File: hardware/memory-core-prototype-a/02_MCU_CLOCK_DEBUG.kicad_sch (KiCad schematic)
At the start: 1 part, among them J902 SHEET_INTERFACE_NOT_FITTED

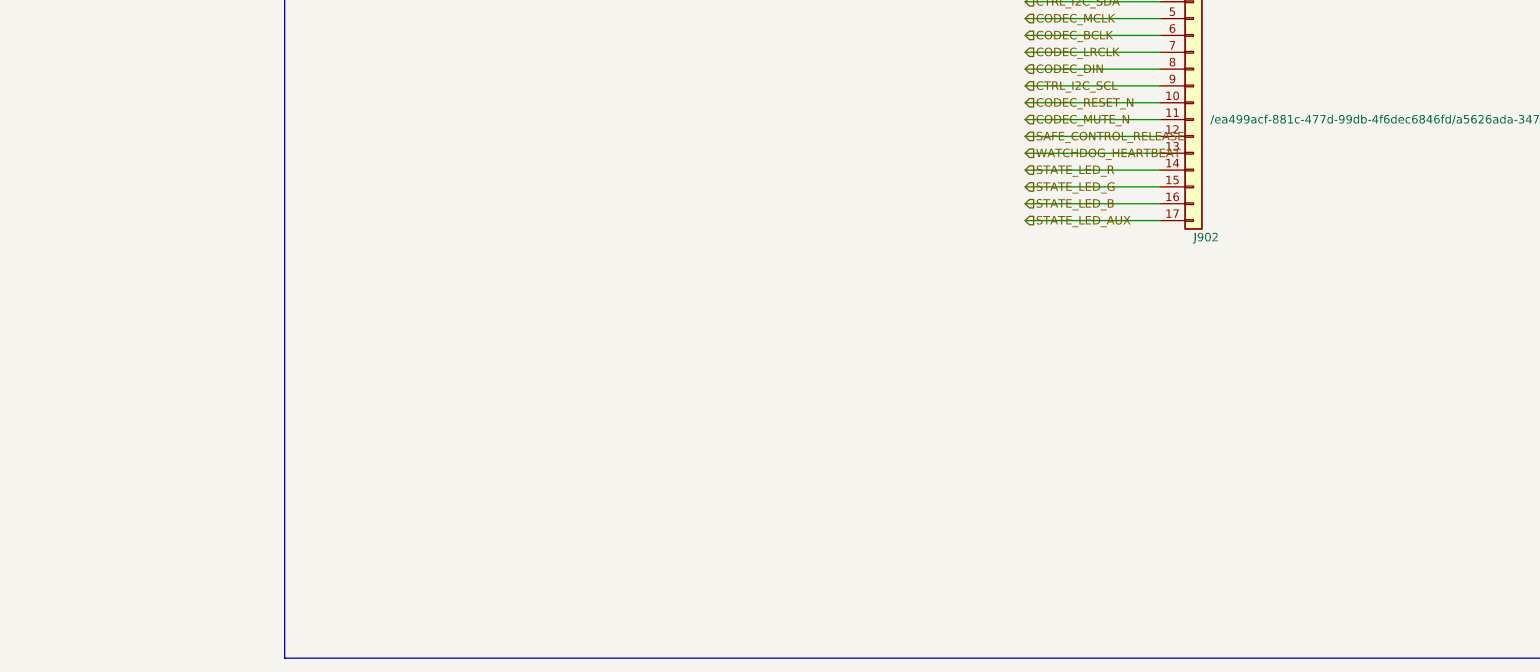
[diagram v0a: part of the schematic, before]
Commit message: Capture ERC-validated controls and state sheet
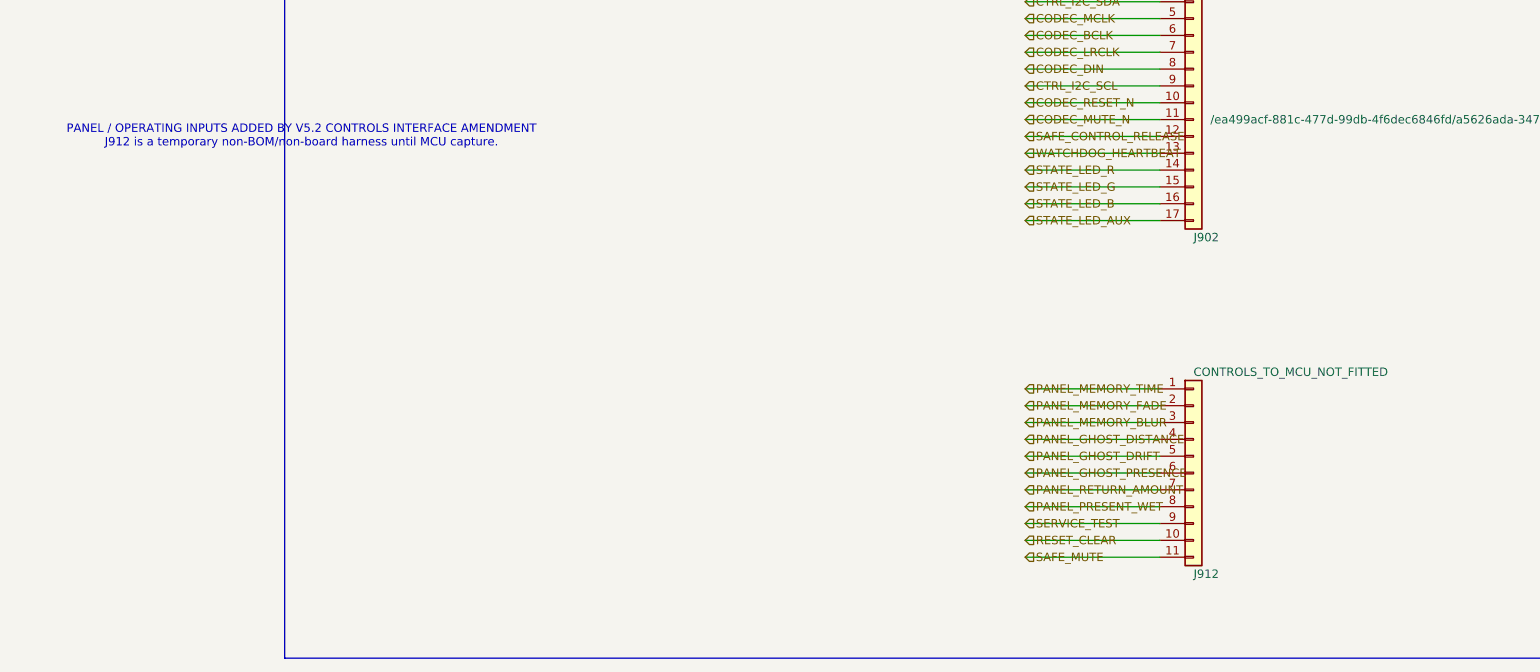
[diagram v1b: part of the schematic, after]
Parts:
- added J912: CONTROLS_TO_MCU_NOT_FITTED, symbol Connector_Generic:Conn_01x11
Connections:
- new net PANEL_GHOST_DISTANCE: J912.4 (Pin_4)
- new net PANEL_GHOST_DRIFT: J912.5 (Pin_5)
- new net PANEL_GHOST_PRESENCE: J912.6 (Pin_6)
- new net PANEL_MEMORY_BLUR: J912.3 (Pin_3)
- new net PANEL_MEMORY_FADE: J912.2 (Pin_2)
- new net PANEL_MEMORY_TIME: J912.1 (Pin_1)
- new net PANEL_PRESENT_WET: J912.8 (Pin_8)
- new net PANEL_RETURN_AMOUNT: J912.7 (Pin_7)
- new net RESET_CLEAR: J912.10 (Pin_10)
- new net SAFE_MUTE: J912.11 (Pin_11)
- new net SERVICE_TEST: J912.9 (Pin_9)
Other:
- note added: "PANEL / OPERATING INPUTS ADDED BY V5.2 CONTROLS INTERFACE AMENDMENT J912 is a temporary non-BOM/non-board harness until MCU capture."

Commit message: Capture ERC-validated MCU clock and debug sheet
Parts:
- removed J902: SHEET_INTERFACE_NOT_FITTED, symbol Connector_Generic:Conn_01x17
- removed J912: CONTROLS_TO_MCU_NOT_FITTED, symbol Connector_Generic:Conn_01x11
- added C201, C202, C203, C204, C205, C208, C211, C212: 100nF, Capacitor_SMD:C_0805_2012Metric, symbol Device:C
- added C206: 4.7µF, Capacitor_SMD:C_0805_2012Metric, symbol Device:C
- added C207: 1µF, Capacitor_SMD:C_0805_2012Metric, symbol Device:C
- added C209, C210: 2.2µF low-ESR, Capacitor_SMD:C_0805_2012Metric, symbol Device:C
- added FB20: 600Ω@100MHz provisional, symbol Device:L_Ferrite
- added J20: SWD SERVICE, symbol Connector_Generic:Conn_01x05
- added R200: 33Ω series, Resistor_SMD:R_0805_2012Metric, symbol Device:R
- added R201: 100k reset default low, Resistor_SMD:R_0805_2012Metric, symbol Device:R
- added R202: 100k mute default low, Resistor_SMD:R_0805_2012Metric, symbol Device:R
- added R203: 100k BOOT0 pull-down, Resistor_SMD:R_0805_2012Metric, symbol Device:R
- added TP200: HSE_24M576, symbol Connector:TestPoint
- added TP201: BOOT0, symbol Connector:TestPoint
- added TP202: CODEC_MCLK, symbol Connector:TestPoint
- added TP203: CODEC_BCLK, symbol Connector:TestPoint
- added TP204: CODEC_LRCLK, symbol Connector:TestPoint
- added TP205: CODEC_DIN, symbol Connector:TestPoint
- added TP206: CODEC_DOUT, symbol Connector:TestPoint
- added TP207: I2C_SCL, symbol Connector:TestPoint
- added TP208: I2C_SDA, symbol Connector:TestPoint
- added TP209: WATCHDOG_HEARTBEAT, symbol Connector:TestPoint
- added TP210: FAULT_RESET_N, symbol Connector:TestPoint
- added TP211: SAFE_RELEASE, symbol Connector:TestPoint
- added TP212: MCU_ANALOG_3V3, symbol Connector:TestPoint
- added U10: STM32H743VIT6, symbol MerrinLab_PrototypeA:STM32H743VIT6_LQFP100
- added U11: 24.576MHz 3V3 CMOS OSC, symbol MerrinLab_PrototypeA:OSC_CMOS_4PIN
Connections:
- net CODEC_BCLK: now also TP203.1, U10.4 (PE5)
- net CODEC_DIN: now also TP205.1, U10.5 (PE6)
- net CODEC_DOUT: now also TP206.1, U10.2 (PE3)
- net CODEC_LRCLK: now also TP204.1, U10.3 (PE4)
- net CODEC_MCLK: now also TP202.1, U10.1 (PE2)
- net CODEC_MUTE_N: now also R202.1, U10.56 (PD9)
- net CODEC_RESET_N: now also R201.1, U10.55 (PD8)
- net CTRL_I2C_SCL: now also TP207.1, U10.95 (PB8)
- net CTRL_I2C_SDA: now also TP208.1, U10.96 (PB9)
- net HARDWARE_FAULT_N: now also J20.4 (Pin_4), TP210.1, U10.14 (NRST), U10.57 (PD10)
- net PANEL_GHOST_DISTANCE: now also U10.25 (PA3)
- net PANEL_GHOST_DRIFT: now also U10.28 (PA4)
- net PANEL_GHOST_PRESENCE: now also U10.29 (PA5)
- net PANEL_MEMORY_BLUR: now also U10.24 (PA2)
- net PANEL_MEMORY_FADE: now also U10.23 (PA1)
- net PANEL_MEMORY_TIME: now also U10.22 (PA0)
- net PANEL_PRESENT_WET: now also U10.31 (PA7)
- net PANEL_RETURN_AMOUNT: now also U10.30 (PA6)
- net RAIL_3V3: now also C201.1, C202.1, C203.1, C204.1, C205.1, C206.1, C211.1, C212.1, FB20.1, J20.1 (Pin_1), U10.100 (VDD), U10.11 (VDD), U10.27 (VDD), U10.50 (VDD), U10.6 (VBAT), U10.75 (VDD), U11.1 (EN), U11.4 (VDD)
- net RESET_CLEAR: now also U10.61 (PD14)
- net SAFE_CONTROL_RELEASE: now also TP211.1, U10.59 (PD12)
- net SAFE_MUTE: now also U10.62 (PD15)
- net SERVICE_TEST: now also U10.60 (PD13)
- net STATE_LED_AUX: now also U10.66 (PC9)
- net STATE_LED_B: now also U10.65 (PC8)
- net STATE_LED_G: now also U10.64 (PC7)
- net STATE_LED_R: now also U10.63 (PC6)
- net WATCHDOG_HEARTBEAT: now also TP209.1, U10.58 (PD11)
- new net BOOT0: R203.1, TP201.1, U10.94 (BOOT0)
- new net GND: C201.2, C202.2, C203.2, C204.2, C205.2, C206.2, C207.2, C208.2, C209.2, C210.2, C211.2, C212.2, J20.5 (Pin_5), R201.2, R202.2, R203.2, U10.10 (VSS), U10.19 (VSSA), U10.26 (VSS), U10.49 (VSS), U10.74 (VSS), U10.99 (VSS), U11.2 (GND)
- new net HSE_IN: R200.2, TP200.1, U10.12 (PH0-OSC_IN)
- new net HSE_OSC_OUT: R200.1, U11.3 (OUT)
- new net MCU_ANALOG_3V3: C207.1, C208.1, FB20.2, TP212.1, U10.20 (VREF+), U10.21 (VDDA)
- new net SWCLK: J20.3 (Pin_3), U10.76 (PA14)
- new net SWDIO: J20.2 (Pin_2), U10.72 (PA13)
- new net VCAP1: C209.1, U10.48 (VCAP1)
- new net VCAP2: C210.1, U10.73 (VCAP2)
- no-connect marks 0 -> 52
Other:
- note added: "All unused LQFP-100 GPIOs are explicitly no-connect. The accepted allocation is encoded by physical pin number, not symbol position."
- note added: "HSE bypass mode: U11 drives PH0-OSC_IN through R200; PH1-OSC_OUT is explicitly unused. 24.576 MHz is within the STM32H743 4–48 MHz external HSE range."
- note added: "STM32H743VIT6 • 24.576 MHz HSE BYPASS • SAI1 TDM • I²C1 • SWD"
- note added: "U10 and U11 footprints intentionally blank. Final decoupling placement, oscillator part, LQFP land pattern and SWD connector remain footprint/mechanical gate items."
- note removed: "HIERARCHY / INTERFACE CAPTURE ONLY — CIRCUIT CONTENT NOT YET ACCEPTED"
- note removed: "PANEL / OPERATING INPUTS ADDED BY V5.2 CONTROLS INTERFACE AMENDMENT J912 is a temporary non-BOM/non-board harness until MCU capture."
- title: Memory Core Prototype A — MCU / CLOCK / DEBUG -> Memory Core Prototype A — MCU / Clock / Debug

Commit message: Complete final integrated schematic review
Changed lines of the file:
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@@
 	)
 	(hierarchical_label "CTRL_I2C_SDA"
-		(shape input)
+		(shape bidirectional)
 		(at 20.32 49.53 0.0000)
 		(effects
@@
 	)
 	(hierarchical_label "CODEC_MCLK"
-		(shape input)
+		(shape output)
 		(at 391.16 30.48 0.0000)
 		(effects
@@
 	)
 	(hierarchical_label "CODEC_BCLK"
-		(shape input)
+		(shape output)
 		(at 391.16 36.83 0.0000)
 		(effects
@@
 	)
 	(hierarchical_label "CODEC_LRCLK"
-		(shape input)
+		(shape output)
 		(at 391.16 43.18 0.0000)
 		(effects
@@
 	)
 	(hierarchical_label "CODEC_DIN"
-		(shape input)
+		(shape output)
 		(at 391.16 49.53 0.0000)
 		(effects
@@
 	)
 	(hierarchical_label "CTRL_I2C_SCL"
-		(shape input)
+		(shape output)
 		(at 391.16 55.88 0.0000)
 		(effects
@@
 	)
 	(hierarchical_label "CODEC_RESET_N"
-		(shape input)
+		(shape output)
 		(at 391.16 62.23 0.0000)
 		(effects
@@
 	)
 	(hierarchical_label "CODEC_MUTE_N"
-		(shape input)
+		(shape output)
 		(at 391.16 68.58 0.0000)
 		(effects
@@
 	)
 	(hierarchical_label "SAFE_CONTROL_RELEASE"
-		(shape input)
+		(shape output)
 		(at 391.16 74.93 0.0000)
 		(effects
@@
 	)
 	(hierarchical_label "WATCHDOG_HEARTBEAT"
-		(shape input)
+		(shape output)
 		(at 391.16 81.28 0.0000)
 		(effects
@@
 	)
 	(hierarchical_label "STATE_LED_R"
-		(shape input)
+		(shape output)
 		(at 391.16 87.63 0.0000)
 		(effects
@@
 	)
 	(hierarchical_label "STATE_LED_G"
-		(shape input)
+		(shape output)
 		(at 391.16 93.98 0.0000)
 		(effects
@@
 	)
 	(hierarchical_label "STATE_LED_B"
-		(shape input)
+		(shape output)
 		(at 391.16 100.33 0.0000)
 		(effects
@@
 	)
 	(hierarchical_label "STATE_LED_AUX"
-		(shape input)
+		(shape output)
 		(at 391.16 106.68 0.0000)
 		(effects
